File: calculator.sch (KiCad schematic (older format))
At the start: 66 parts, among them SW49 AC, SW50 ON, U2 SN74F1056, U3 SN74F1056, U4 SN74F1056, U5 SN74F1056, U6 SN74F1056, U7 SN74F1056

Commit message: added lots of stuff to the schematic
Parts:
- removed R10, R3, R4, R5, R6, R7, R8, R9: R, ~, symbol R
- removed SW1, SW10, SW11, SW12, SW13, SW14, SW15, SW16, SW17, SW18, SW19, SW2, SW20, SW21, SW22, SW23, SW24, SW25, SW26, SW27, SW28, SW29, SW3, SW30, SW31, SW32, SW33, SW34, SW35, SW36, SW37, SW38, SW39, SW4, SW40, SW41, SW42, SW43, SW44, SW45, SW46, SW47, SW48, SW5, SW6, SW7, SW8, SW9: ~, ~, symbol SW_PUSH_SMALL
- removed U2, U3, U4, U5, U6, U7: SN74F1056, ~, symbol SN74F1056
- added U1: AT89C51RC2_SMD, symbol AT89C51RC2_SMD
- added U10: 74LS573, symbol 74LS573
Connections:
- net labels added: A0, A1, A10, A11, A12, A13, A14, A15, A2, A3, A4, A5, A6, A7, A8, A9, D0, D1, D2, D3, D4, D5, D6, D7, GND
- wire segments 149 -> 100
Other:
- moved on the sheet: R1, R2, SW49, SW50

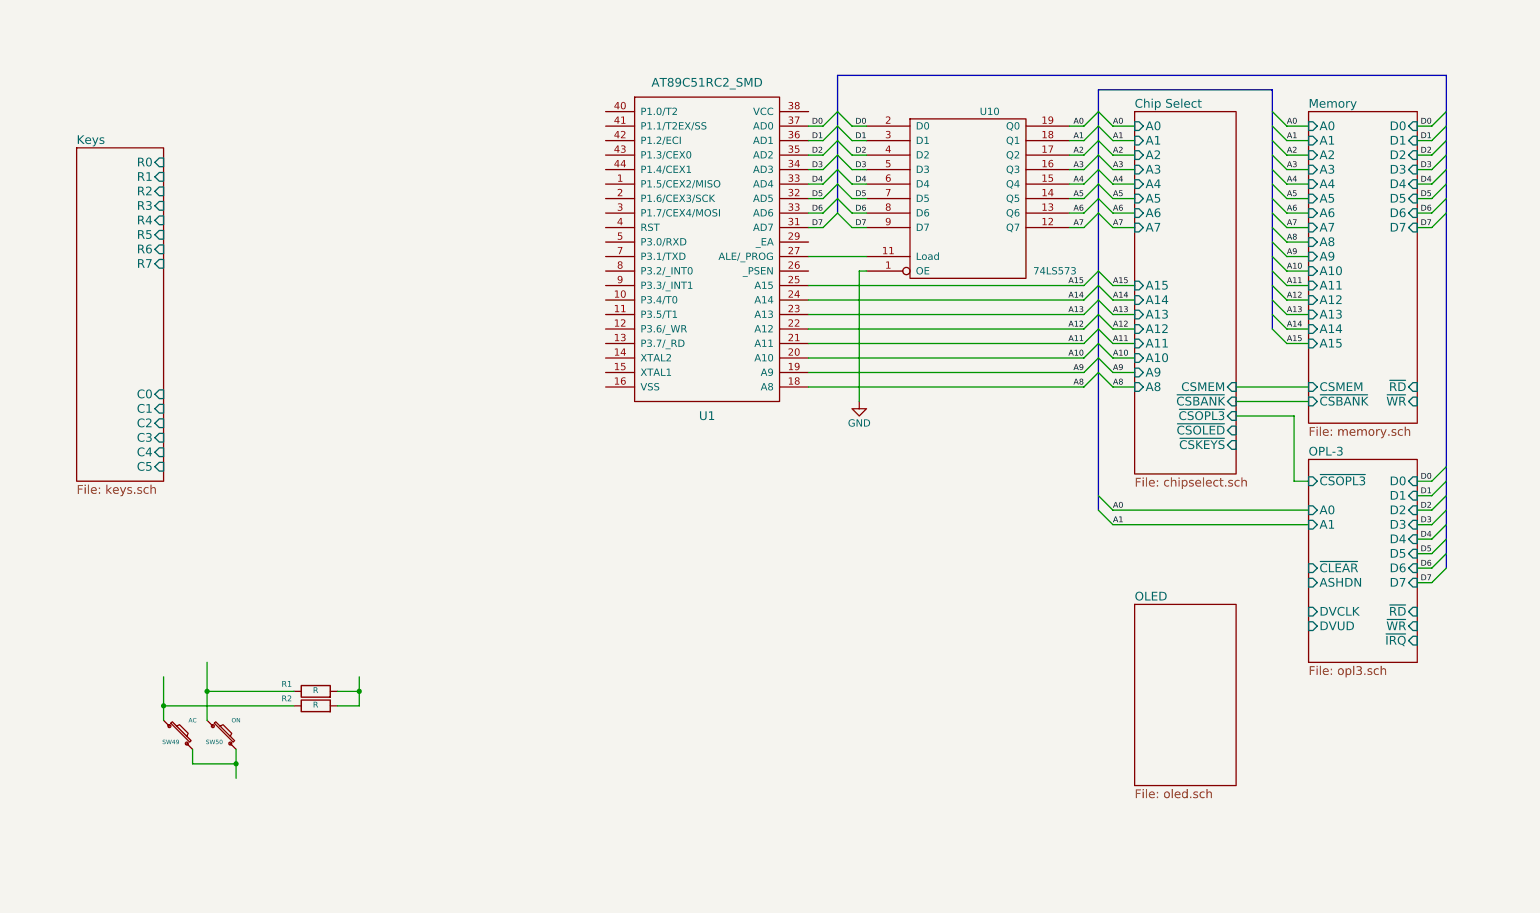
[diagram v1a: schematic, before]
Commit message: add more circuitry to schematic
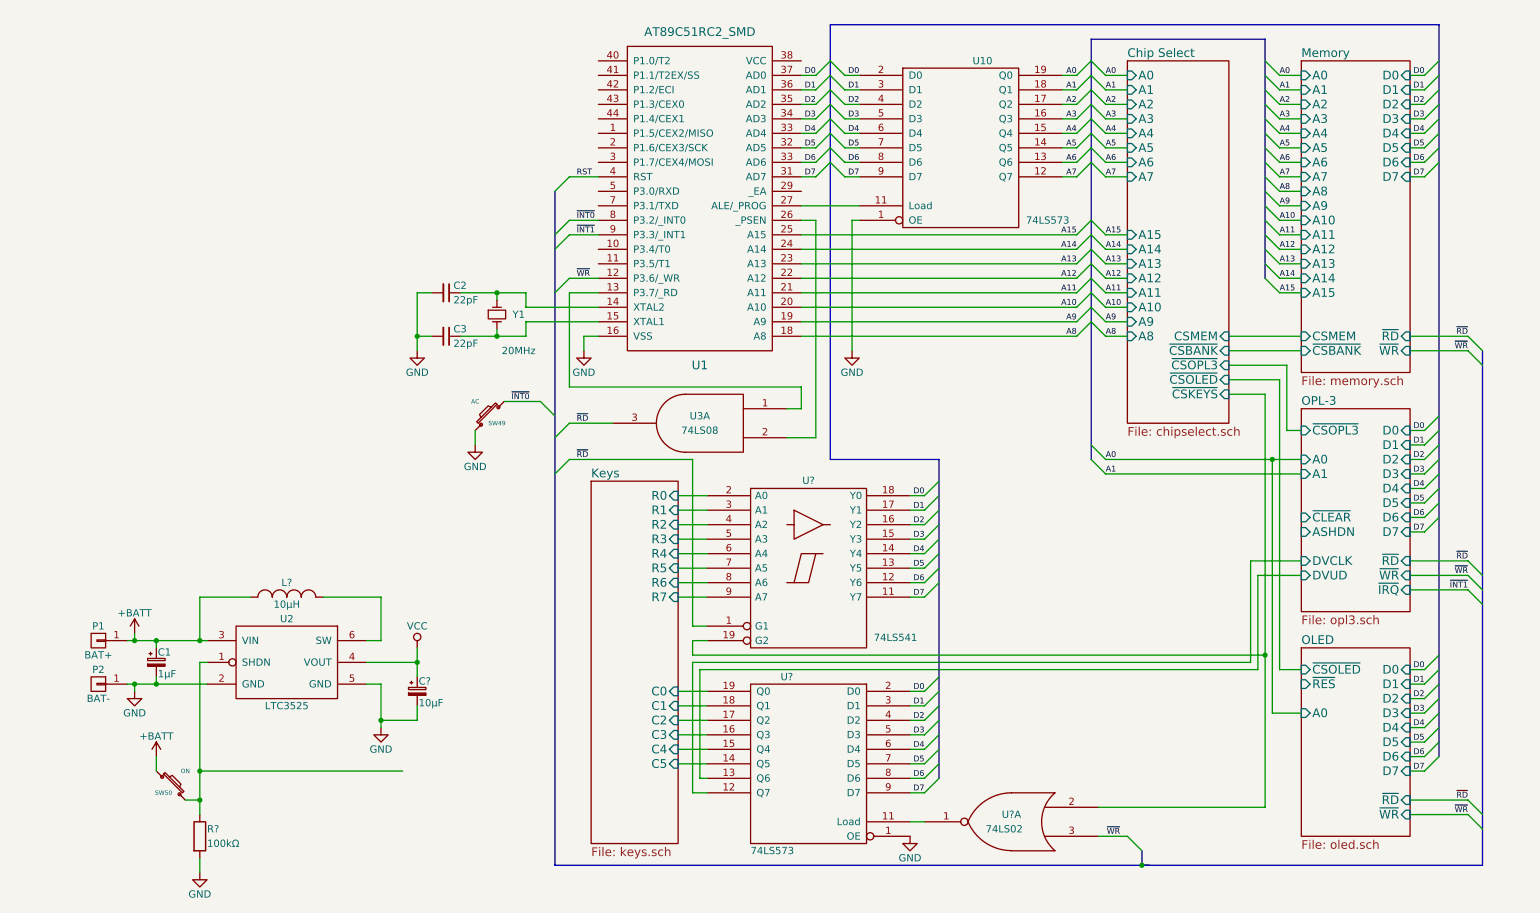
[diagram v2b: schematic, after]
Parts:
- removed R1, R2: R, ~, symbol R
- added C1: 1µF, symbol CP_Small
- added C2, C3: 22pF, symbol C_Small
- added C?: 10µF, symbol CP_Small
- added L?: 10µH, symbol INDUCTOR_SMALL
- added P1: BAT+, symbol CONN_01X01
- added P2: BAT-, symbol CONN_01X01
- added R?: 100kΩ, symbol R
- added U2: LTC3525, symbol LTC3525
- added U3: 74LS08, symbol 74LS08
- added U?: 74LS573, symbol 74LS573
- added U?: 74LS541, symbol 74LS541
- added U?: 74LS02, symbol 74LS02
- added Y1: 20MHz, symbol Crystal_Small
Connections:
- net labels added: +BATT, RST, VCC, ~INT0, ~INT1, ~RD, ~WR
- wire segments 100 -> 212
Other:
- moved on the sheet: SW49, SW50, U1, U10
